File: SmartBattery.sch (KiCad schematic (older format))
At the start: 5 parts, among them J1 USB_C_Receptacle_USB2.0, J2 ST-USB-003A, J3 Barrel_Jack_MountingPin, U6 ESP32-WROOM-32U, U7 ATSAMD21G18A-MU

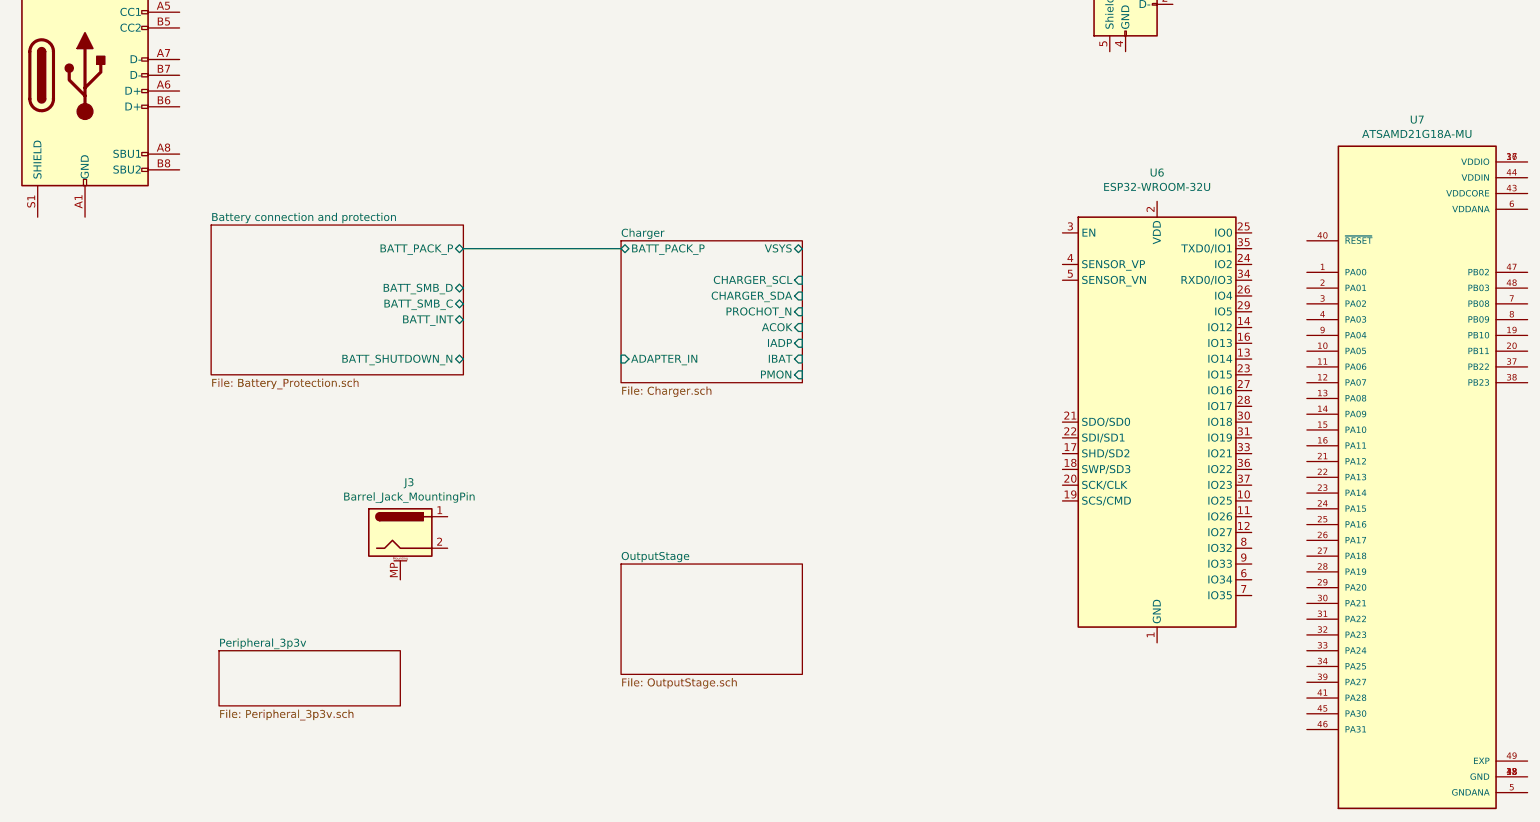
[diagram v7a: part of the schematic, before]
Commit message: Switching over to jlpcb
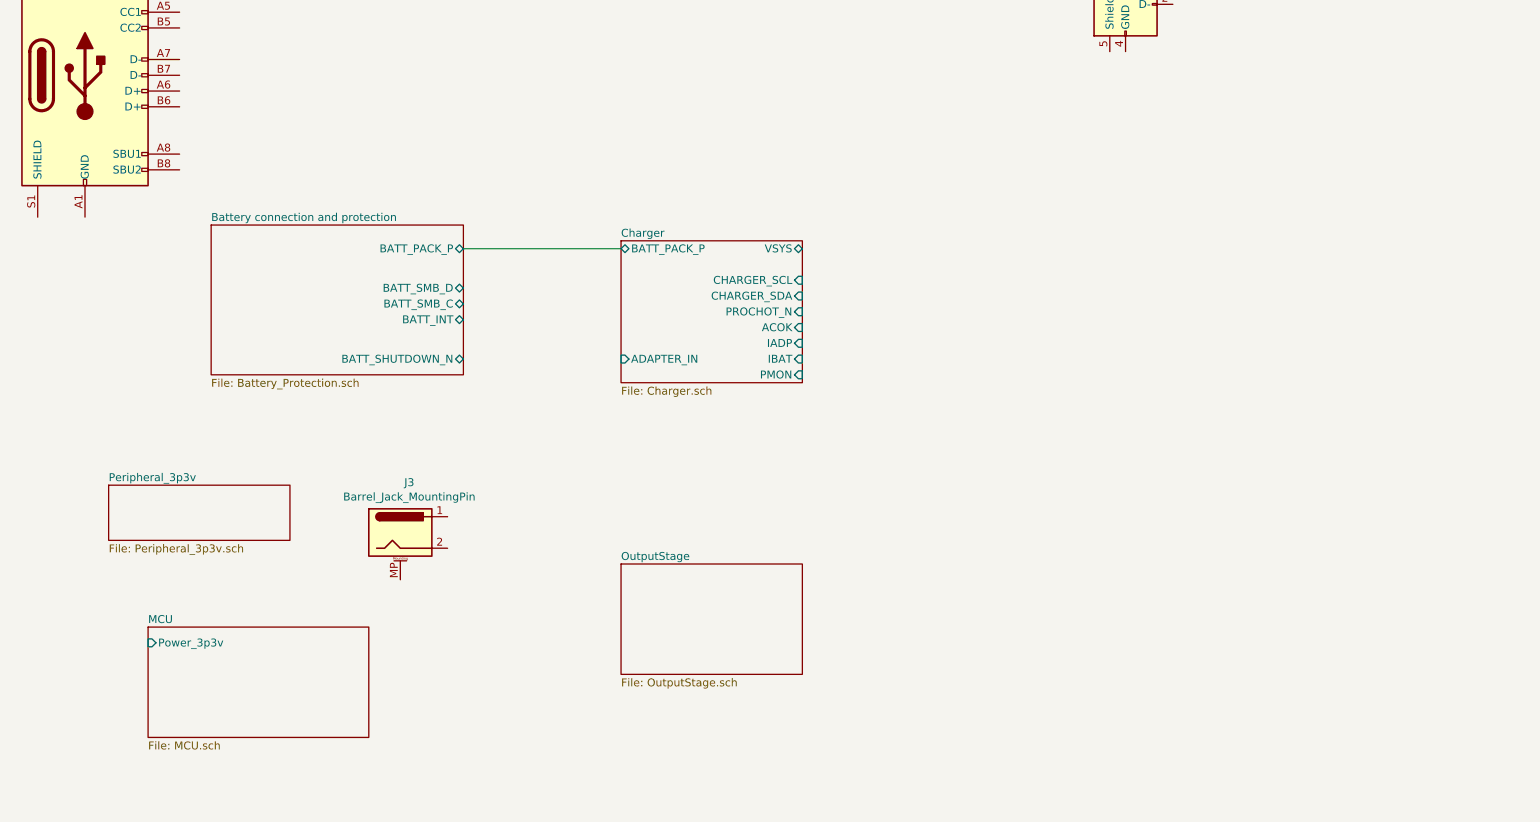
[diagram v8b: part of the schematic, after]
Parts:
- removed U6: ESP32-WROOM-32U, RF_Module:ESP32-WROOM-32U, symbol RF_Module:ESP32-WROOM-32U
- removed U7: ATSAMD21G18A-MU, SmartBattery:QFN50P700X700X90-49N, symbol SmartBattery:ATSAMD21G18A-MU
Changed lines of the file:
@@
 $Descr A4 11693 8268
 encoding utf-8
-Sheet 1 5
+Sheet 1 6
 Title ""
 Date ""
@@
 $EndSheet
 $Sheet
-S 2150 5450 1150 350
+S 1450 4400 1150 350
 U 6041786F
 F0 "Peripheral_3p3v" 50
 F1 "Peripheral_3p3v.sch" 50
 $EndSheet
-$Comp
-L RF_Module:ESP32-WROOM-32U U6
-U 1 1 5FE15F32
-P 8100 4000
-F 0 "U6" H 8100 5581 50  0000 C CNN
-F 1 "ESP32-WROOM-32U" H 8100 5490 50  0000 C CNN
-F 2 "RF_Module:ESP32-WROOM-32U" H 8100 2500 50  0001 C CNN
-F 3 "https://www.espressif.com/sites/default/files/documentation/esp32-wroom-32d_esp32-wroom-32u_datasheet_en.pdf" H 7800 4050 50  0001 C CNN
-F 4 "ESP32-WROOM-32U" H 8100 4000 50  0001 C CNN "SKU"
-	1    8100 4000
-	1    0    0    -1
-$EndComp
-$Comp
-L SmartBattery:ATSAMD21G18A-MU U7
-U 1 1 5FE17BB1
-P 9750 4350
-F 0 "U7" H 9750 6617 50  0000 C CNN
-F 1 "ATSAMD21G18A-MU" H 9750 6526 50  0000 C CNN
-F 2 "SmartBattery:QFN50P700X700X90-49N" H 9750 4350 50  0001 L BNN
-F 3 "" H 9750 4350 50  0001 L BNN
-F 4 "ATSAMD21G18A-MU" H 9750 4350 50  0001 L BNN "MP"
-F 5 "QFN-48 Microchip" H 9750 4350 50  0001 L BNN "PACKAGE"
-F 6 "Good" H 9750 4350 50  0001 L BNN "AVAILABILITY"
-F 7 "IPC-7351B" H 9750 4350 50  0001 L BNN "STANDARD"
-F 8 "2.99 USD" H 9750 4350 50  0001 L BNN "PRICE"
-F 9 "Cortex-M0+, 256KB FLASH, 32KB SRAM, USB, DMA, T&R - 48QFN IND TEMP, GREEN, 1.6-3.6V, 48MHz/ QFN _ZA_" H 9750 4350 50  0001 L BNN "DESCRIPTION"
-F 10 "Microchip" H 9750 4350 50  0001 L BNN "MF"
-F 11 "310010095" H 9750 4350 50  0001 C CNN "SKU"
-	1    9750 4350
-	1    0    0    -1
-$EndComp
 $Comp
 L Connector:USB_C_Receptacle_USB2.0 J1
@@
 	1    0    0    -1
 $EndComp
+$Sheet
+S 1700 5300 1400 700
+U 5FF1D194
+F0 "MCU" 50
+F1 "MCU.sch" 50
+F2 "Power_3p3v" I L 1700 5400 50
+$EndSheet
 $EndSCHEMATC
